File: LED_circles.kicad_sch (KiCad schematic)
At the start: 0 parts

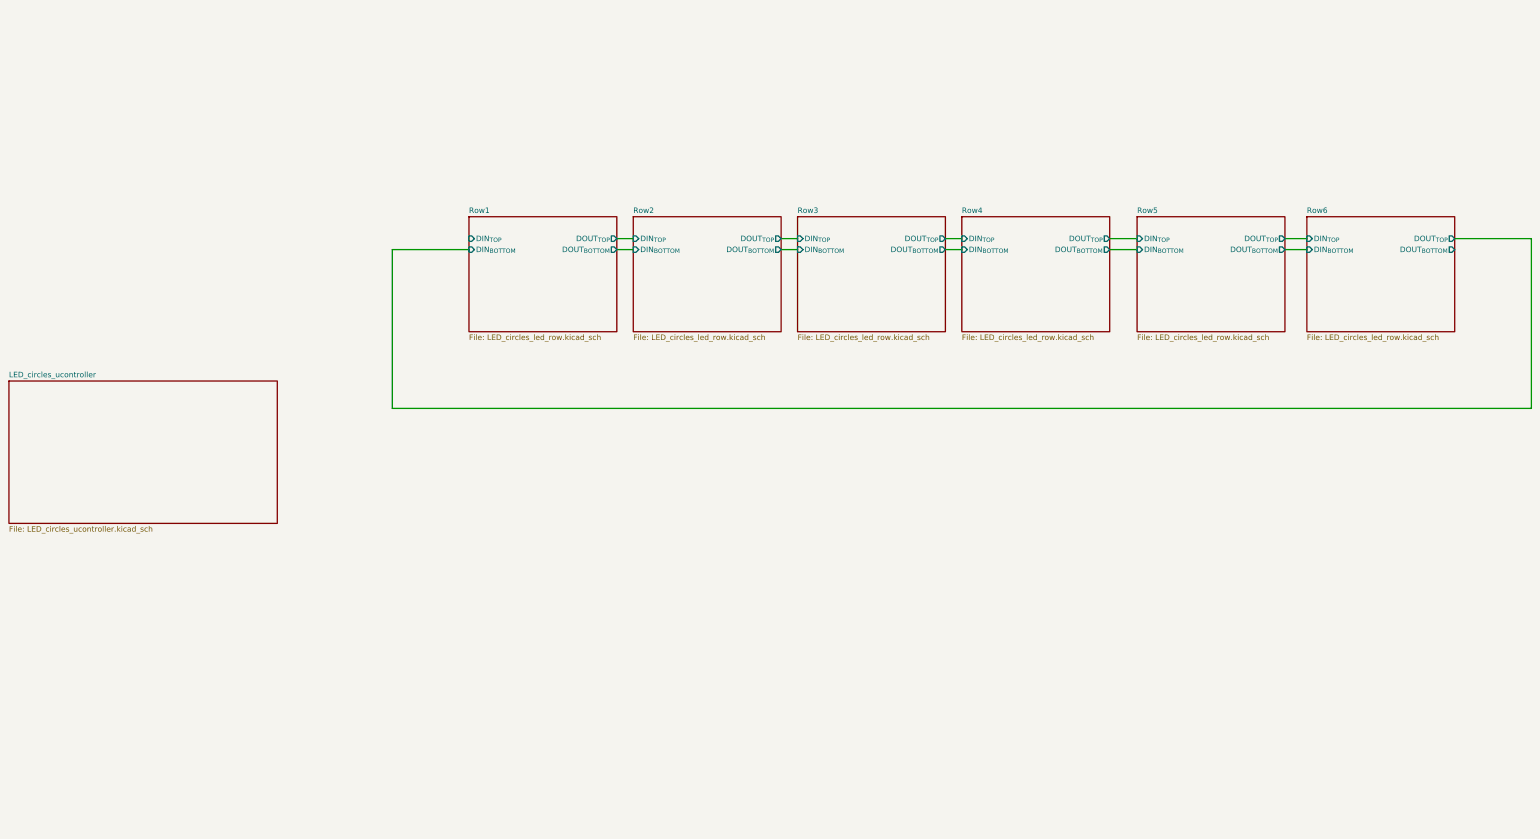
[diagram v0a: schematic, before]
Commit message: Initial Schematic and LED Placement
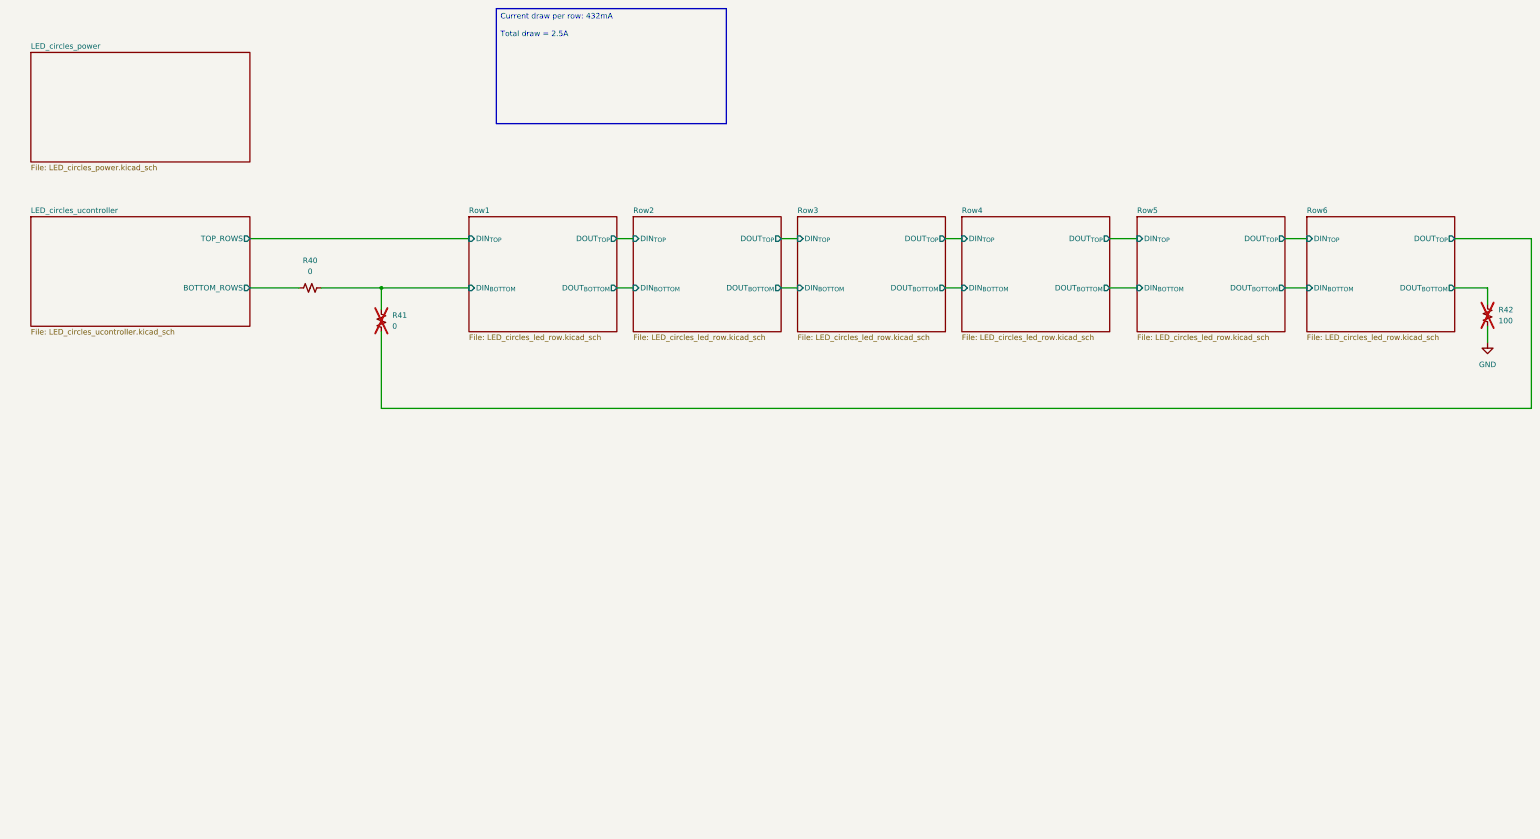
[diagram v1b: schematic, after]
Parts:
- added R40, R41: 0, Resistor_SMD:R_0805_2012Metric, symbol Device:R_Small_US
- added R42: 100, Resistor_SMD:R_0805_2012Metric, symbol Device:R_Small_US
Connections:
- net Row1/DIN_{BOTTOM}: now also R40.1, R41.1
- net Row6/DOUT_{BOTTOM}: now also R42.1
- new net GND: R42.2
- new net LED_circles_ucontroller/BOTTOM_ROWS: R40.2
- new net Row6/DOUT_{TOP}: R41.2
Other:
- added sheet LED_circles_power (LED_circles_power.kicad_sch)
- sheet LED_circles_ucontroller ports: added BOTTOM_ROWS, TOP_ROWS; removed none

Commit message: Initial layout of top layer
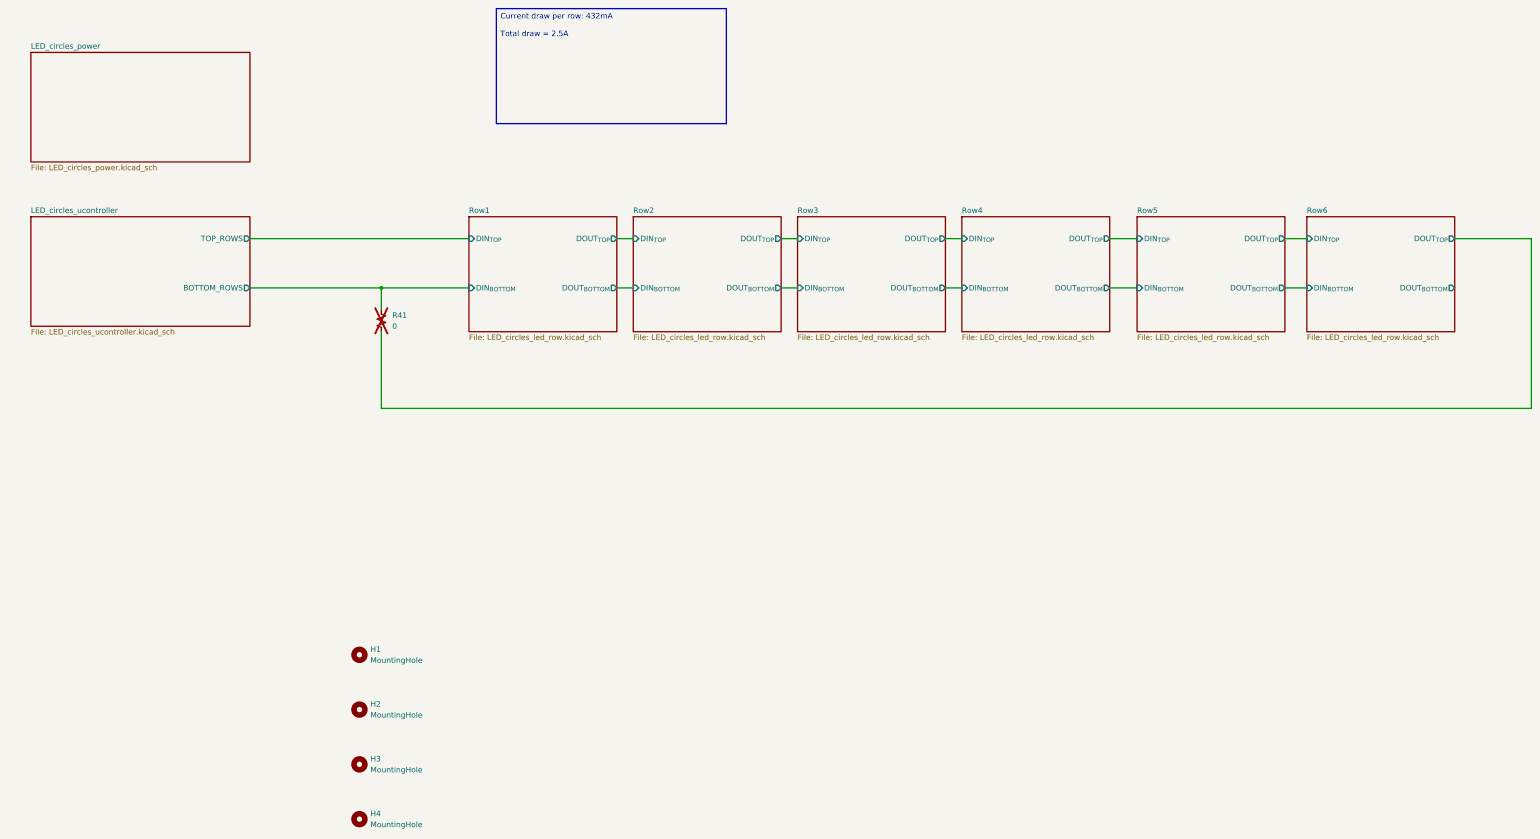
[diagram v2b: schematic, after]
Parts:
- removed R40: 0, Resistor_SMD:R_0805_2012Metric, symbol Device:R_Small_US
- removed R42: 100, Resistor_SMD:R_0805_2012Metric, symbol Device:R_Small_US
- added H1, H2, H3, H4: MountingHole, MountingHole:MountingHole_2.5mm, symbol Mechanical:MountingHole
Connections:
- net Row1/DIN_{BOTTOM} is gone; now on net LED_circles_ucontroller/BOTTOM_ROWS: R41.1
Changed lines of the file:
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@@
-	(wire
-		(pts
-			(xy 355.6 105.41) (xy 363.22 105.41)
-		)
-		(stroke
-			(width 0)
-			(type default)
-		)
-	)
 	(wire
 		(pts
@@
 	(wire
 		(pts
-			(xy 363.22 105.41) (xy 363.22 109.22)
-		)
-		(stroke
-			(width 0)
-			(type default)
-		)
-	)
-	(wire
-		(pts
-			(xy 92.71 105.41) (xy 106.68 105.41)
-		)
-		(stroke
-			(width 0)
-			(type default)
-		)
-	)
-	(wire
-		(pts
-			(xy 363.22 114.3) (xy 363.22 118.11)
-		)
-		(stroke
-			(width 0)
-			(type default)
-		)
-	)
-	(wire
-		(pts
 			(xy 316.23 105.41) (xy 321.31 105.41)
 		)
@@
 	(wire
 		(pts
-			(xy 76.2 105.41) (xy 87.63 105.41)
+			(xy 76.2 105.41) (xy 106.68 105.41)
 		)
 		(stroke
@@
 	)
 	(symbol
-		(lib_id "Device:R_Small_US")
-		(at 363.22 111.76 0)
+		(lib_id "Mechanical:MountingHole")
+		(at 101.6 215.9 0)
 		(unit 1)
 		(exclude_from_sim no)
-		(in_bom yes)
-		(on_board yes)
-		(dnp yes)
-		(fields_autoplaced yes)
-		(property "Reference" "R42"
-			(at 365.76 110.4899 0)
-			(effects
-				(font
-					(size 1.27 1.27)
-				)
-				(justify left)
-			)
-		)
-		(property "Value" "100"
-			(at 365.76 113.0299 0)
-			(effects
-				(font
-					(size 1.27 1.27)
-				)
-				(justify left)
-			)
-		)
-		(property "Footprint" "Resistor_SMD:R_0805_2012Metric"
-			(at 363.22 111.76 0)
-			(effects
-				(font
-					(size 1.27 1.27)
-				)
-				(hide yes)
-			)
-		)
-		(property "Datasheet" "~"
-			(at 363.22 111.76 0)
-			(effects
-				(font
-					(size 1.27 1.27)
-				)
-				(hide yes)
-			)
-		)
-		(property "Description" "Resistor, small US symbol"
-			(at 363.22 111.76 0)
-			(effects
-				(font
-					(size 1.27 1.27)
-				)
-				(hide yes)
-			)
-		)
-		(pin "1"
-		)
-		(pin "2"
-		)
-		(instances
-			(project "LED_circles"
-				(path "/fee5cc62-df5b-4e25-a1c9-d9673ac3b8e2"
-					(reference "R42")
-					(unit 1)
-				)
-			)
-		)
-	)
-	(symbol
-		(lib_id "Device:R_Small_US")
-		(at 90.17 105.41 270)
-		(unit 1)
-		(exclude_from_sim no)
-		(in_bom yes)
+		(in_bom no)
 		(on_board yes)
 		(dnp no)
 		(fields_autoplaced yes)
-		(property "Reference" "R40"
-			(at 90.17 99.06 90)
-			(effects
-				(font
-					(size 1.27 1.27)
-				)
-			)
-		)
-		(property "Value" "0"
-			(at 90.17 101.6 90)
-			(effects
-				(font
-					(size 1.27 1.27)
-				)
-			)
-		)
-		(property "Footprint" "Resistor_SMD:R_0805_2012Metric"
-			(at 90.17 105.41 0)
+		(property "Reference" "H3"
+			(at 104.14 214.6299 0)
+			(effects
+				(font
+					(size 1.27 1.27)
+				)
+				(justify left)
+			)
+		)
+		(property "Value" "MountingHole"
+			(at 104.14 217.1699 0)
+			(effects
+				(font
+					(size 1.27 1.27)
+				)
+				(justify left)
+			)
+		)
+		(property "Footprint" "MountingHole:MountingHole_2.5mm"
+			(at 101.6 215.9 0)
 			(effects
 				(font
@@
 		)
 		(property "Datasheet" "~"
-			(at 90.17 105.41 0)
-			(effects
-				(font
-					(size 1.27 1.27)
-				)
-				(hide yes)
-			)
-		)
-		(property "Description" "Resistor, small US symbol"
-			(at 90.17 105.41 0)
-			(effects
-				(font
-					(size 1.27 1.27)
-				)
-				(hide yes)
-			)
-		)
-		(pin "1"
-		)
-		(pin "2"
+			(at 101.6 215.9 0)
+			(effects
+				(font
+					(size 1.27 1.27)
+				)
+				(hide yes)
+			)
+		)
+		(property "Description" "Mounting Hole without connection"
+			(at 101.6 215.9 0)
+			(effects
+				(font
+					(size 1.27 1.27)
+				)
+				(hide yes)
+			)
 		)
 		(instances
 			(project ""
 				(path "/fee5cc62-df5b-4e25-a1c9-d9673ac3b8e2"
-					(reference "R40")
+					(reference "H3")
 					(unit 1)
 				)
@@
 	)
 	(symbol
-		(lib_id "power:GND")
-		(at 363.22 118.11 0)
+		(lib_id "Mechanical:MountingHole")
+		(at 101.6 190.5 0)
 		(unit 1)
 		(exclude_from_sim no)
-		(in_bom yes)
+		(in_bom no)
 		(on_board yes)
 		(dnp no)
 		(fields_autoplaced yes)
-		(property "Reference" "#PWR0162"
-			(at 363.22 124.46 0)
-			(effects
-				(font
-					(size 1.27 1.27)
-				)
-				(hide yes)
-			)
-		)
-		(property "Value" "GND"
-			(at 363.22 123.19 0)
-			(effects
-				(font
-					(size 1.27 1.27)
-				)
-			)
-		)
-		(property "Footprint" ""
-			(at 363.22 118.11 0)
-			(effects
-				(font
-					(size 1.27 1.27)
-				)
-				(hide yes)
-			)
-		)
-		(property "Datasheet" ""
-			(at 363.22 118.11 0)
-			(effects
-				(font
-					(size 1.27 1.27)
-				)
-				(hide yes)
-			)
-		)
-		(property "Description" "Power symbol creates a global label with name \"GND\" , ground"
-			(at 363.22 118.11 0)
-			(effects
-				(font
-					(size 1.27 1.27)
-				)
-				(hide yes)
-			)
-		)
-		(pin "1"
+		(property "Reference" "H1"
+			(at 104.14 189.2299 0)
+			(effects
+				(font
+					(size 1.27 1.27)
+				)
+				(justify left)
+			)
+		)
+		(property "Value" "MountingHole"
+			(at 104.14 191.7699 0)
+			(effects
+				(font
+					(size 1.27 1.27)
+				)
+				(justify left)
+			)
+		)
+		(property "Footprint" "MountingHole:MountingHole_2.5mm"
+			(at 101.6 190.5 0)
+			(effects
+				(font
+					(size 1.27 1.27)
+				)
+				(hide yes)
+			)
+		)
+		(property "Datasheet" "~"
+			(at 101.6 190.5 0)
+			(effects
+				(font
+					(size 1.27 1.27)
+				)
+				(hide yes)
+			)
+		)
+		(property "Description" "Mounting Hole without connection"
+			(at 101.6 190.5 0)
+			(effects
+				(font
+					(size 1.27 1.27)
+				)
+				(hide yes)
+			)
 		)
 		(instances
 			(project ""
 				(path "/fee5cc62-df5b-4e25-a1c9-d9673ac3b8e2"
-					(reference "#PWR0162")
+					(reference "H1")
+					(unit 1)
+				)
+			)
+		)
+	)
+	(symbol
+		(lib_id "Mechanical:MountingHole")
+		(at 101.6 203.2 0)
+		(unit 1)
+		(exclude_from_sim no)
+		(in_bom no)
+		(on_board yes)
+		(dnp no)
+		(fields_autoplaced yes)
+		(property "Reference" "H2"
+			(at 104.14 201.9299 0)
+			(effects
+				(font
+					(size 1.27 1.27)
+				)
+				(justify left)
+			)
+		)
+		(property "Value" "MountingHole"
+			(at 104.14 204.4699 0)
+			(effects
+				(font
+					(size 1.27 1.27)
+				)
+				(justify left)
+			)
+		)
+		(property "Footprint" "MountingHole:MountingHole_2.5mm"
+			(at 101.6 203.2 0)
+			(effects
+				(font
+					(size 1.27 1.27)
+				)
+				(hide yes)
+			)
+		)
+		(property "Datasheet" "~"
+			(at 101.6 203.2 0)
+			(effects
+				(font
+					(size 1.27 1.27)
+				)
+				(hide yes)
+			)
+		)
+		(property "Description" "Mounting Hole without connection"
+			(at 101.6 203.2 0)
+			(effects
+				(font
+					(size 1.27 1.27)
+				)
+				(hide yes)
+			)
+		)
+		(instances
+			(project ""
+				(path "/fee5cc62-df5b-4e25-a1c9-d9673ac3b8e2"
+					(reference "H2")
 					(unit 1)
 				)
@@
 					(unit 1)
 				)
+			)
+		)
+	)
+	(symbol
+		(lib_id "Mechanical:MountingHole")
+		(at 101.6 228.6 0)
+		(unit 1)
+		(exclude_from_sim no)
+		(in_bom no)
+		(on_board yes)
+		(dnp no)
+		(fields_autoplaced yes)
+		(property "Reference" "H4"
+			(at 104.14 227.3299 0)
+			(effects
+				(font
+					(size 1.27 1.27)
+				)
+				(justify left)
+			)
+		)
+		(property "Value" "MountingHole"
+			(at 104.14 229.8699 0)
+			(effects
+				(font
+					(size 1.27 1.27)
+				)
+				(justify left)
+			)
+		)
+		(property "Footprint" "MountingHole:MountingHole_2.5mm"
+			(at 101.6 228.6 0)
+			(effects
+				(font
+					(size 1.27 1.27)
+				)
+				(hide yes)
+			)
+		)
+		(property "Datasheet" "~"
+			(at 101.6 228.6 0)
+			(effects
+				(font
+					(size 1.27 1.27)
+				)
+				(hide yes)
+			)
+		)
+		(property "Description" "Mounting Hole without connection"
+			(at 101.6 228.6 0)
+			(effects
+				(font
+					(size 1.27 1.27)
+				)
+				(hide yes)
+			)
+		)
+		(instances
+			(project ""
+				(path "/fee5cc62-df5b-4e25-a1c9-d9673ac3b8e2"
+					(reference "H4")
+					(unit 1)
+				)

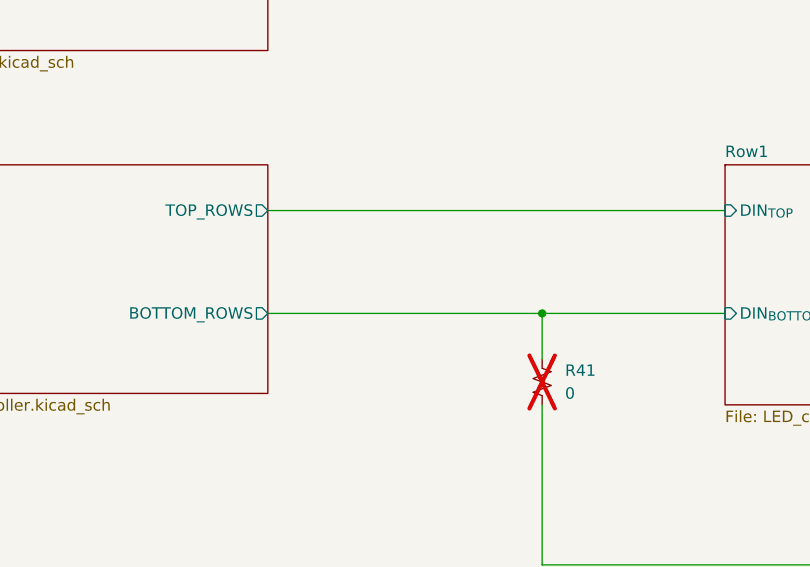
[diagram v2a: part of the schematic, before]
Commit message: Fixed PCB DRC issues.
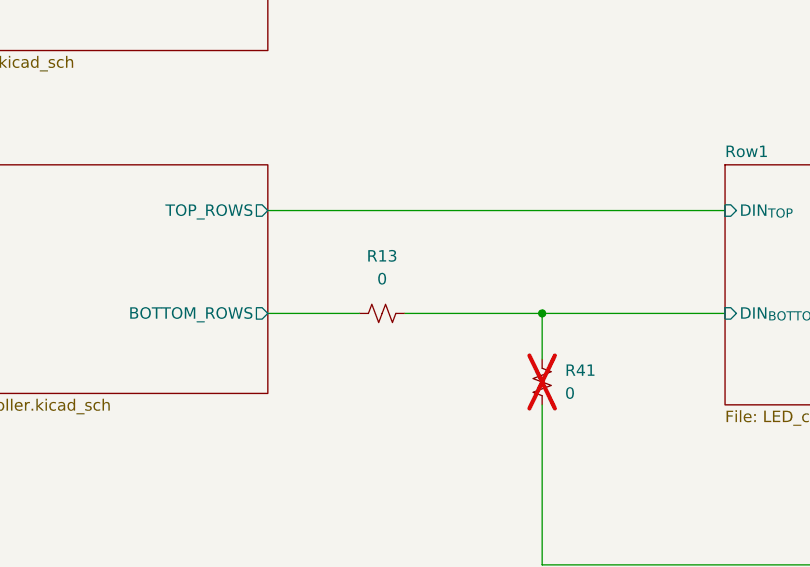
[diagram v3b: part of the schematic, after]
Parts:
- added R13: 0, Resistor_SMD:R_0805_2012Metric, symbol Device:R_Small_US
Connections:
- net LED_circles_ucontroller/BOTTOM_ROWS: now also R13.1; no longer R41.1
- new net Row1/DIN_{BOTTOM}: R13.2, R41.1
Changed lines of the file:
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@@
+	(wire
+		(pts
+			(xy 91.44 105.41) (xy 106.68 105.41)
+		)
+		(stroke
+			(width 0)
+			(type default)
+		)
+	)
 	(wire
 		(pts
@@
 	(wire
 		(pts
-			(xy 76.2 105.41) (xy 106.68 105.41)
+			(xy 76.2 105.41) (xy 86.36 105.41)
 		)
 		(stroke
@@
 		)
 	)
+	(symbol
+		(lib_id "Device:R_Small_US")
+		(at 88.9 105.41 90)
+		(unit 1)
+		(exclude_from_sim no)
+		(in_bom no)
+		(on_board yes)
+		(dnp no)
+		(fields_autoplaced yes)
+		(property "Reference" "R13"
+			(at 88.9 99.06 90)
+			(effects
+				(font
+					(size 1.27 1.27)
+				)
+			)
+		)
+		(property "Value" "0"
+			(at 88.9 101.6 90)
+			(effects
+				(font
+					(size 1.27 1.27)
+				)
+			)
+		)
+		(property "Footprint" "Resistor_SMD:R_0805_2012Metric"
+			(at 88.9 105.41 0)
+			(effects
+				(font
+					(size 1.27 1.27)
+				)
+				(hide yes)
+			)
+		)
+		(property "Datasheet" "~"
+			(at 88.9 105.41 0)
+			(effects
+				(font
+					(size 1.27 1.27)
+				)
+				(hide yes)
+			)
+		)
+		(property "Description" "Resistor, small US symbol"
+			(at 88.9 105.41 0)
+			(effects
+				(font
+					(size 1.27 1.27)
+				)
+				(hide yes)
+			)
+		)
+		(pin "1"
+		)
+		(pin "2"
+		)
+		(instances
+			(project "LED_circles"
+				(path "/fee5cc62-df5b-4e25-a1c9-d9673ac3b8e2"
+					(reference "R13")
+					(unit 1)
+				)
+			)
+		)
+	)
